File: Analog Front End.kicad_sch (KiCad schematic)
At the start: 16 parts, among them SW2 SW_DPST, U1 AD5160, U2 TL074, U4 TL074

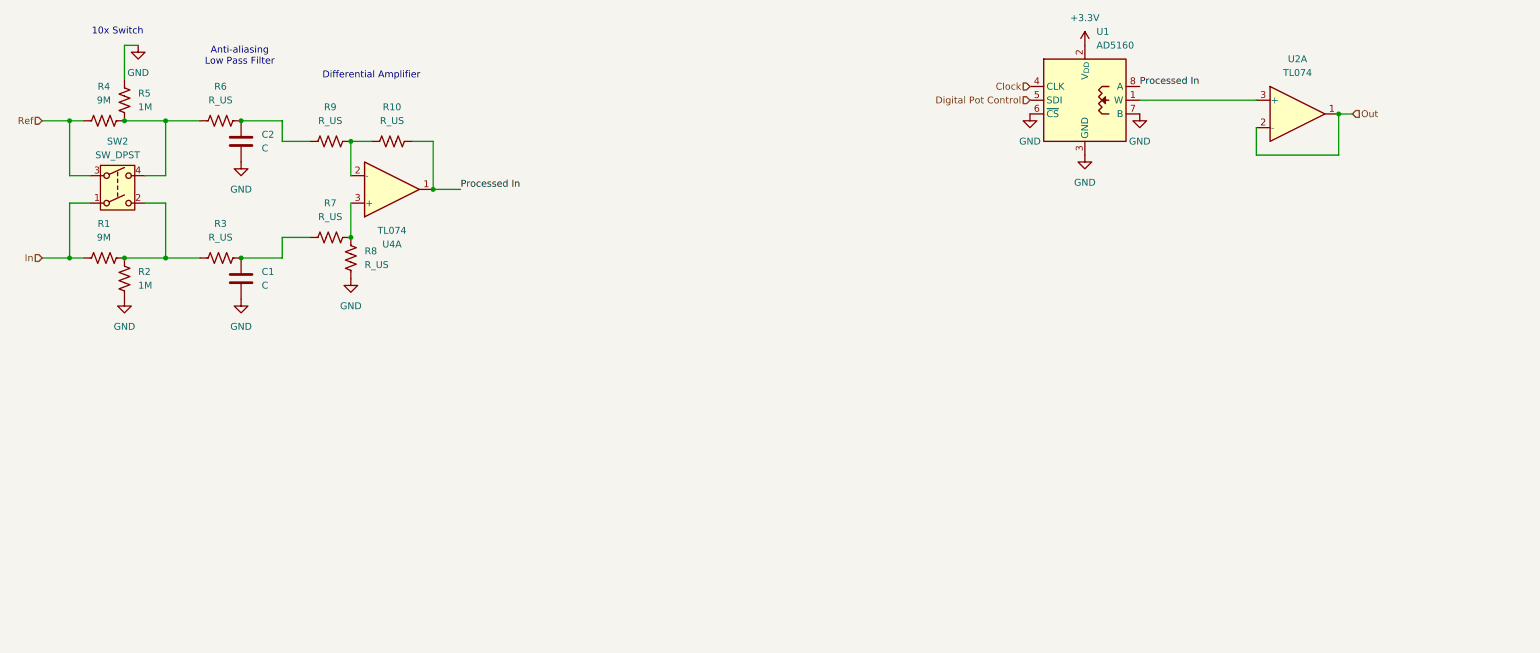
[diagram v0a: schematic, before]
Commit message: fixed 10x voltage divider
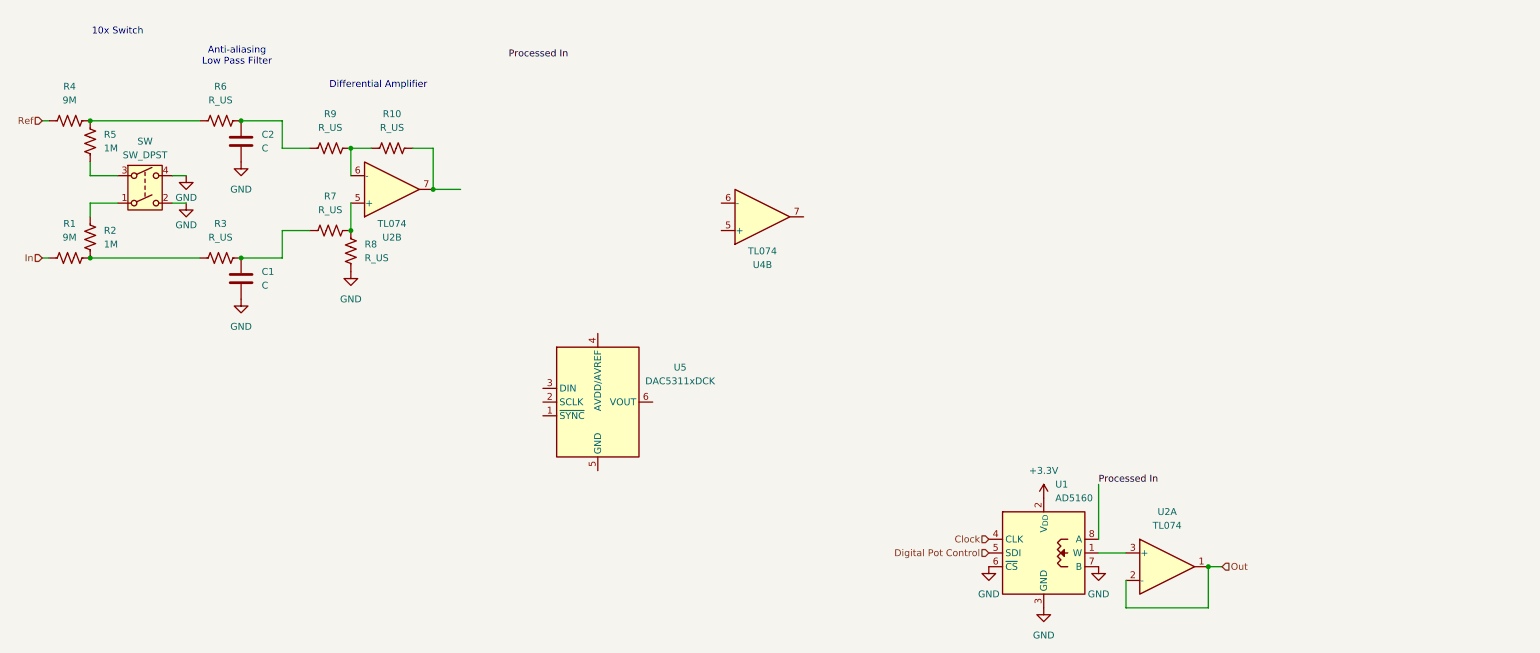
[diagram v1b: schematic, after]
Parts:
- added U4: TL074, symbol Amplifier_Operational:TL074
- added U5: DAC5311xDCK, Package_TO_SOT_SMD:SOT-363_SC-70-6, symbol Analog_DAC:DAC5311xDCK
- renumbered SW2 to SW, U4 to U2
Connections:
- net GND: now also SW.2, SW.4; no longer R2.1, R5.2
- net In: no longer SW.1
- net Processed In: no longer R10.2, U2.1
- net Ref: no longer SW.3
- net at R10.1, R9.2: now also U2.6 (-); no longer U2.2 (-)
- net at R7.2, R8.2: now also U2.5 (+); no longer U2.3 (+)
- net at R1.2, R3.1: now also R2.1; no longer R2.2, SW.2
- net at R4.2, R6.1: now also R5.2; no longer R5.1, SW.4
- new net: R10.2, U2.7
- new net: R2.2, SW.1
- new net: R5.1, SW.3
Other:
- moved on the sheet: R1, R10, R2, R4, R5, R7, R8, R9, SW, U1, U2A

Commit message: added MCU, crystal, and USB-C port
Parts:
- added R11, R12, R13: R_US, symbol Device:R_US
- added unit 4 of U2
- added unit 5 of U2
- renumbered U4 to U2
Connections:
- net +3.3V: now also U5.4 (AVDD/AVREF); no longer U1.2 (V_{DD})
- net Clock: now also U5.2 (SCLK); no longer U1.4 (CLK)
- net Digital Pot Control: no longer U1.5 (SDI)
- net GND: now also U5.5 (GND), U2.12 (+); no longer U1.3 (GND), U1.6 (~{CS}), U1.7 (B)
- net Processed In: now also R13.2, U2.14; no longer U1.8 (A)
- net Filtered Ref: now reaches C2.1, R6.2
- net Filtered Ref: no longer R9.1
- net Filtered In: now reaches C1.1, R3.2
- net Filtered In: no longer R7.1
- net at U1.1 (W): no longer U2.3 (+)
- net at R10.2, U2.7: now also U2.10 (+)
- net DC Offset DAC ~{CS}: now reaches U5.1 (~{SYNC})
- net Offset DAC Control: now reaches U5.3 (DIN)
- net at U5.6 (VOUT): now also R12.1
- new net: R11.1, U2.8, U2.9 (-)
- new net: R11.2, R12.2, R13.1, U2.13 (-)
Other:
- note added: "DC Offset Generator"
- moved on the sheet: C1, C2, R10, R3, R6, R7, R8, R9, U1, U2A, U2B, U2C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
